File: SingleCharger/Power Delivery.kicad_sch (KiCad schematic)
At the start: 32 parts, among them U3 TPS54360BDDAR, U4 TPS54360BDDAR, U5 NCP1117ST33T3G

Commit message: Rebuild
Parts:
- removed C15, C16: 10u, Capacitor_SMD:C_1206_3216Metric, symbol Device:C
- removed U5: NCP1117ST33T3G, COMPONENTS:SOT-223-3_L6.5-W3.4-P2.30-LS7.0-BR, symbol COMPONENTS:NCP1117ST33T3G

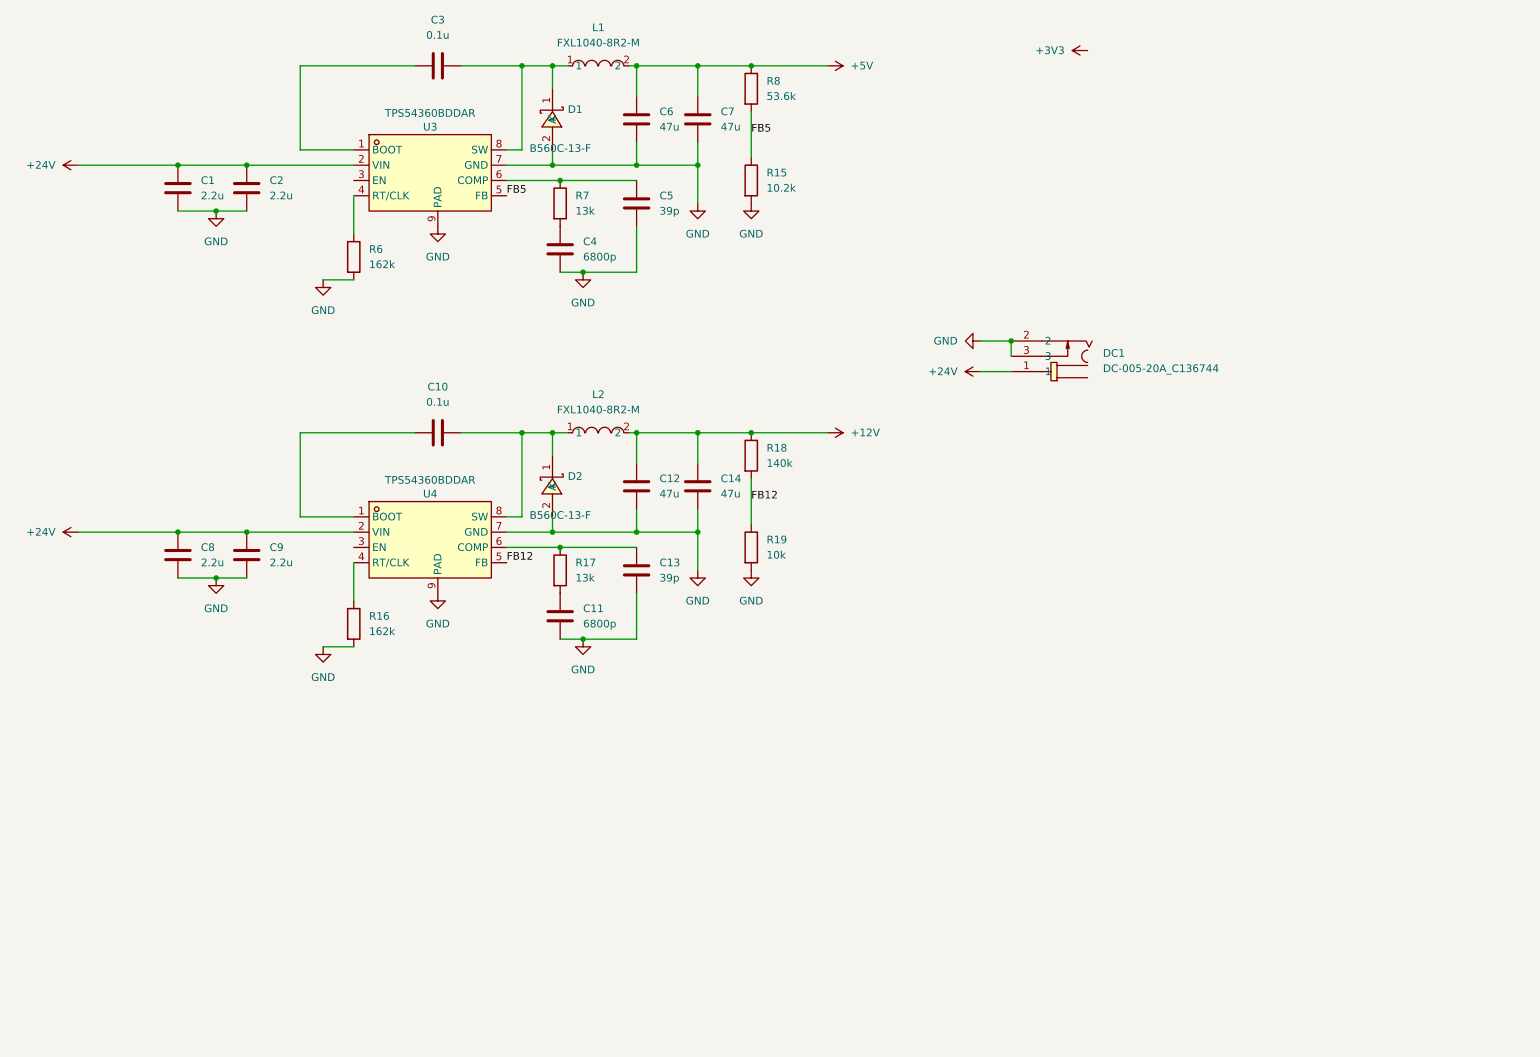
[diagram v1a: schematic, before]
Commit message: Moved to +48V Feed. 25.2 Controlled by Pico.
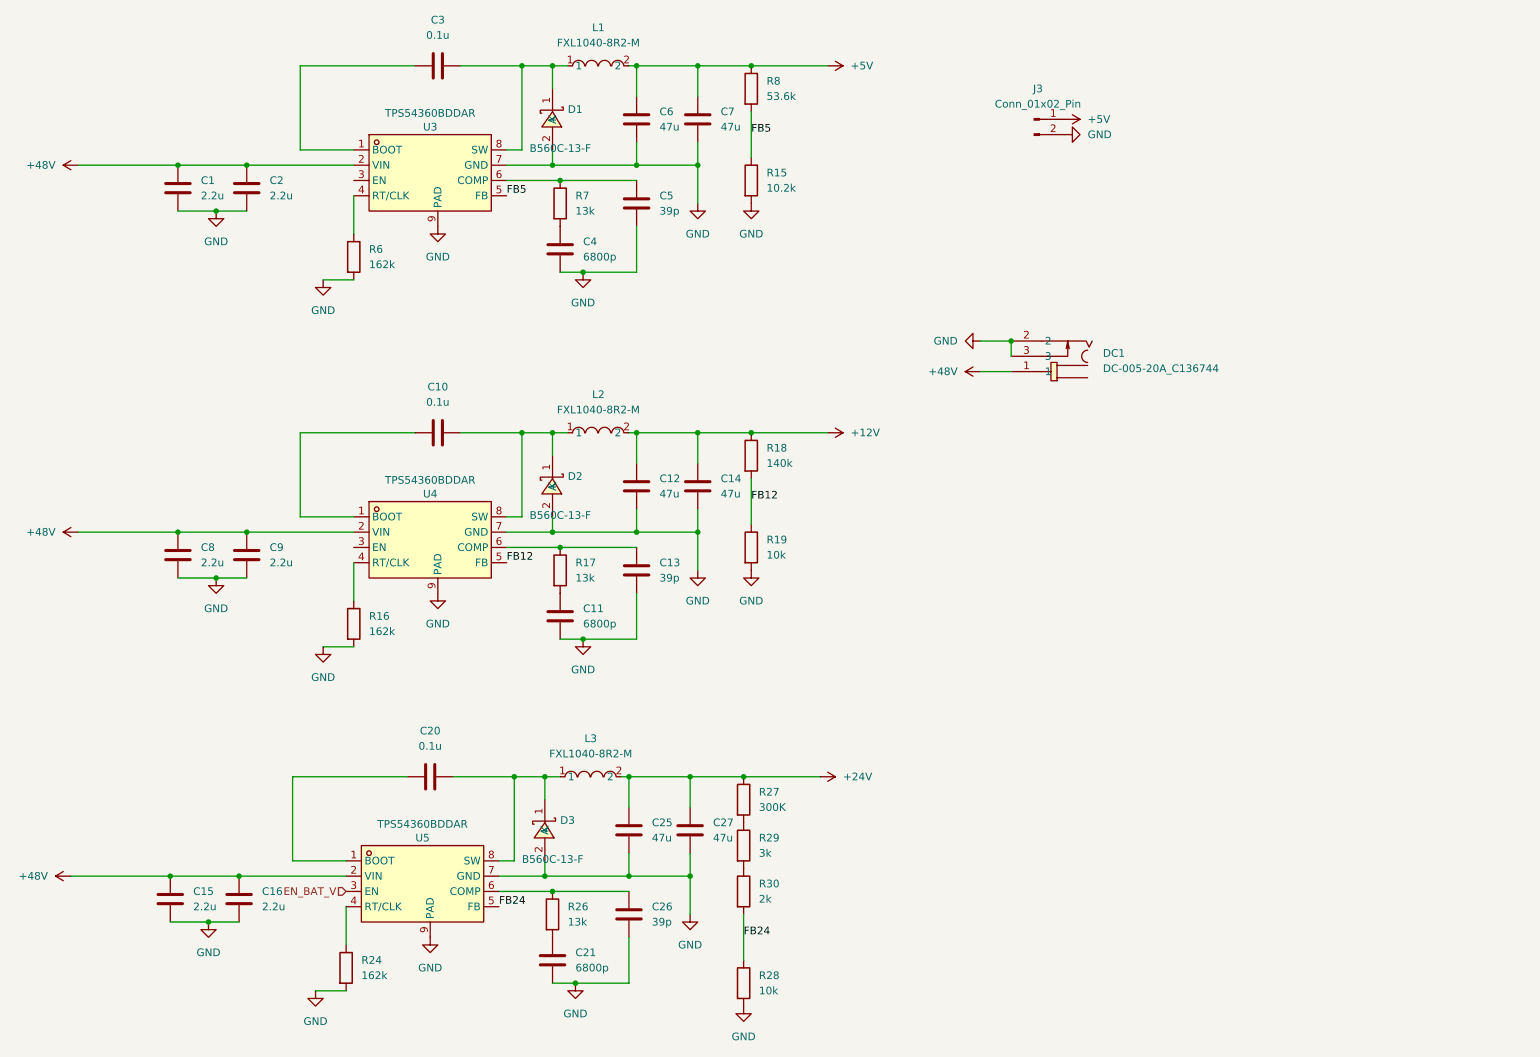
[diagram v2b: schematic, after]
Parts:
- added C15, C16: 2.2u, Capacitor_SMD:C_1206_3216Metric, symbol Device:C
- added C20: 0.1u, Capacitor_SMD:C_1206_3216Metric, symbol Device:C
- added C21: 6800p, Capacitor_SMD:C_1206_3216Metric, symbol Device:C
- added C25, C27: 47u, Capacitor_SMD:C_1206_3216Metric, symbol Device:C
- added C26: 39p, Capacitor_SMD:C_1206_3216Metric, symbol Device:C
- added D3: B560C-13-F, COMPONENTS:SMC_L7.1-W6.2-LS8.1-RD, symbol NEW:B560C-13-F
- added J3: Conn_01x02_Pin, Connector_PinHeader_2.54mm:PinHeader_1x02_P2.54mm_Vertical, symbol Connector:Conn_01x02_Pin
- added L3: FXL1040-8R2-M, COMPONENTS:IND-SMD_L11.5-W10.0_FXL1040, symbol NEW:FXL1040-8R2-M
- added R24: 162k, Resistor_SMD:R_1206_3216Metric_Pad1.30x1.75mm_HandSolder, symbol Device:R
- added R26: 13k, Resistor_SMD:R_1206_3216Metric_Pad1.30x1.75mm_HandSolder, symbol Device:R
- added R27: 300K, Resistor_SMD:R_1206_3216Metric_Pad1.30x1.75mm_HandSolder, symbol Device:R
- added R28: 10k, Resistor_SMD:R_1206_3216Metric_Pad1.30x1.75mm_HandSolder, symbol Device:R
- added R29: 3k, Resistor_SMD:R_1206_3216Metric_Pad1.30x1.75mm_HandSolder, symbol Device:R
- added R30: 2k, Resistor_SMD:R_1206_3216Metric_Pad1.30x1.75mm_HandSolder, symbol Device:R
- added U5: TPS54360BDDAR, COMPONENTS:SOIC-8_L5.0-W4.0-P1.27-LS6.0-BL-EP2.0, symbol NEW:TPS54360BDDAR
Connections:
- net +24V: now also C25.1, C27.1, L3.2, R27.1; no longer C1.1, C2.1, C8.1, C9.1, DC1.1, U3.2 (VIN), U4.2 (VIN)
- net +5V: now also J3.1 (Pin_1)
- net GND: now also C15.2, C16.2, C21.2, C25.2, C26.2, C27.2, D3.2 (A), J3.2 (Pin_2), R24.2, R28.2, U5.7 (GND), U5.9 (PAD)
- new net: C26.1, R26.1, U5.6 (COMP)
- new net: C21.1, R26.2
- new net: C20.2, D3.1 (K), L3.1, U5.8 (SW)
- new net: R27.2, R29.1
- new net: R24.1, U5.4 (RT/CLK)
- new net: R29.2, R30.1
- new net: C20.1, U5.1 (BOOT)
- new net +48V: C1.1, C15.1, C16.1, C2.1, C8.1, C9.1, DC1.1, U3.2 (VIN), U4.2 (VIN), U5.2 (VIN)
- new net EN_BAT_V: U5.3 (EN)
- new net FB24: R28.1, R30.2, U5.5 (FB)
